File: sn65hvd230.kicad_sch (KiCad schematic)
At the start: 1 part, among them U6 SN65HVD230

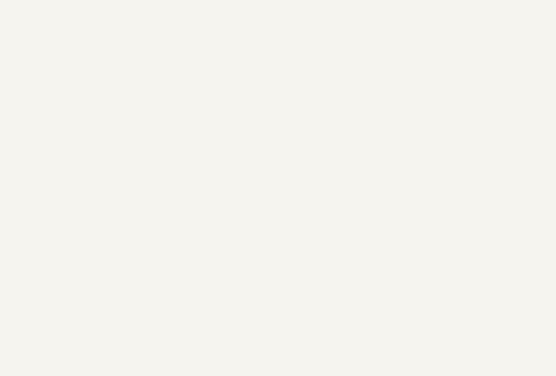
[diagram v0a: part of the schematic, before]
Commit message: feat: done rough board placements for general shape
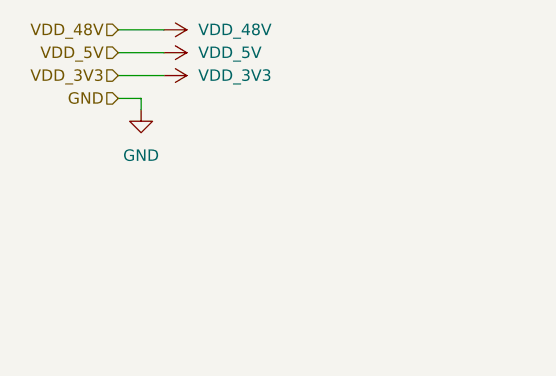
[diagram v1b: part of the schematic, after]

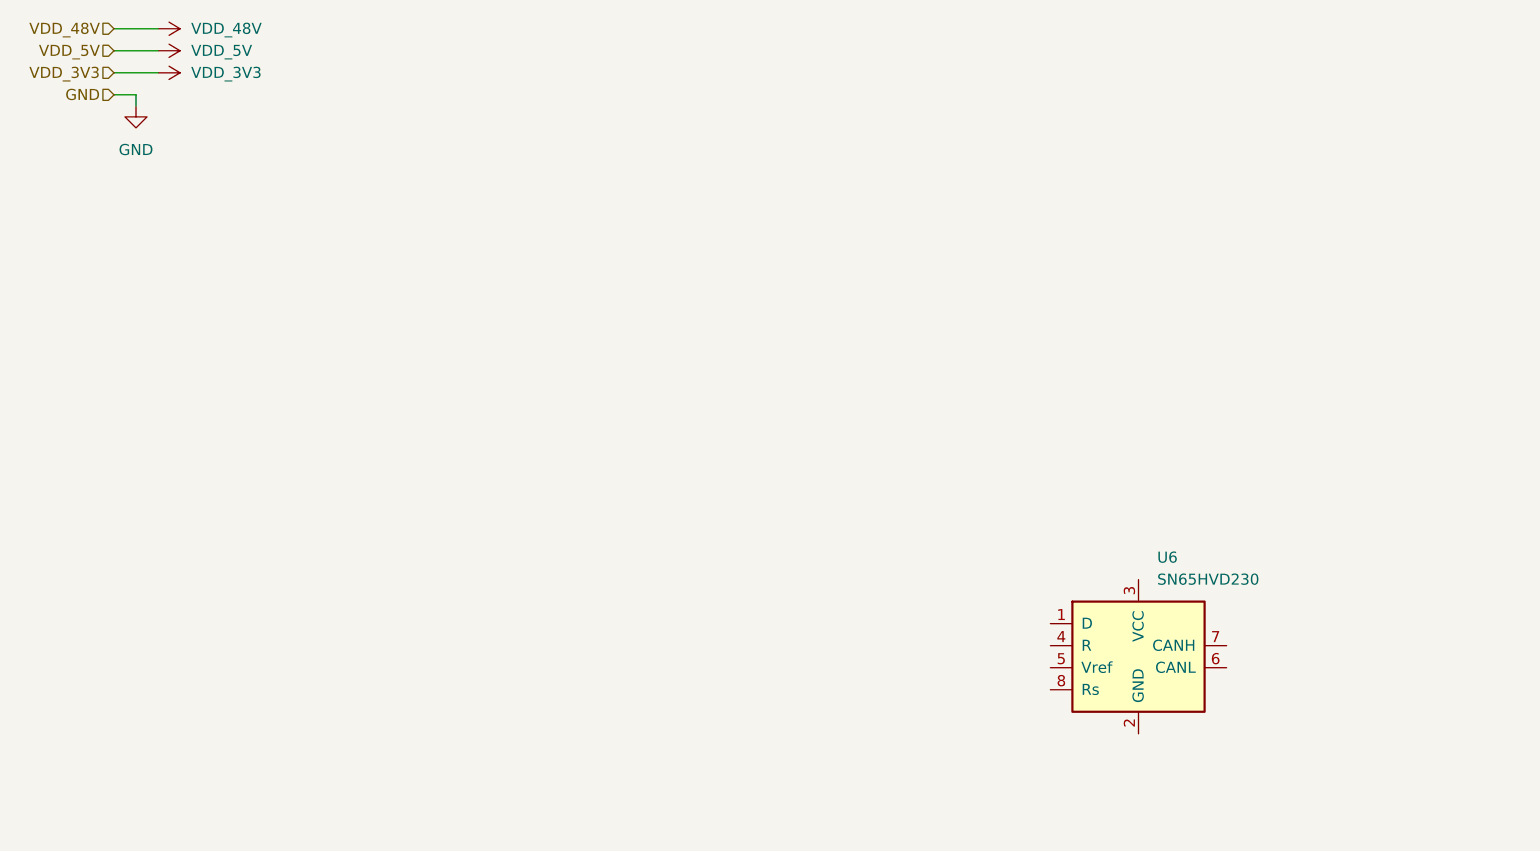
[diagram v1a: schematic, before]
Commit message: fix: fleshignout schematic for mcu, fpga and mag + peripherals
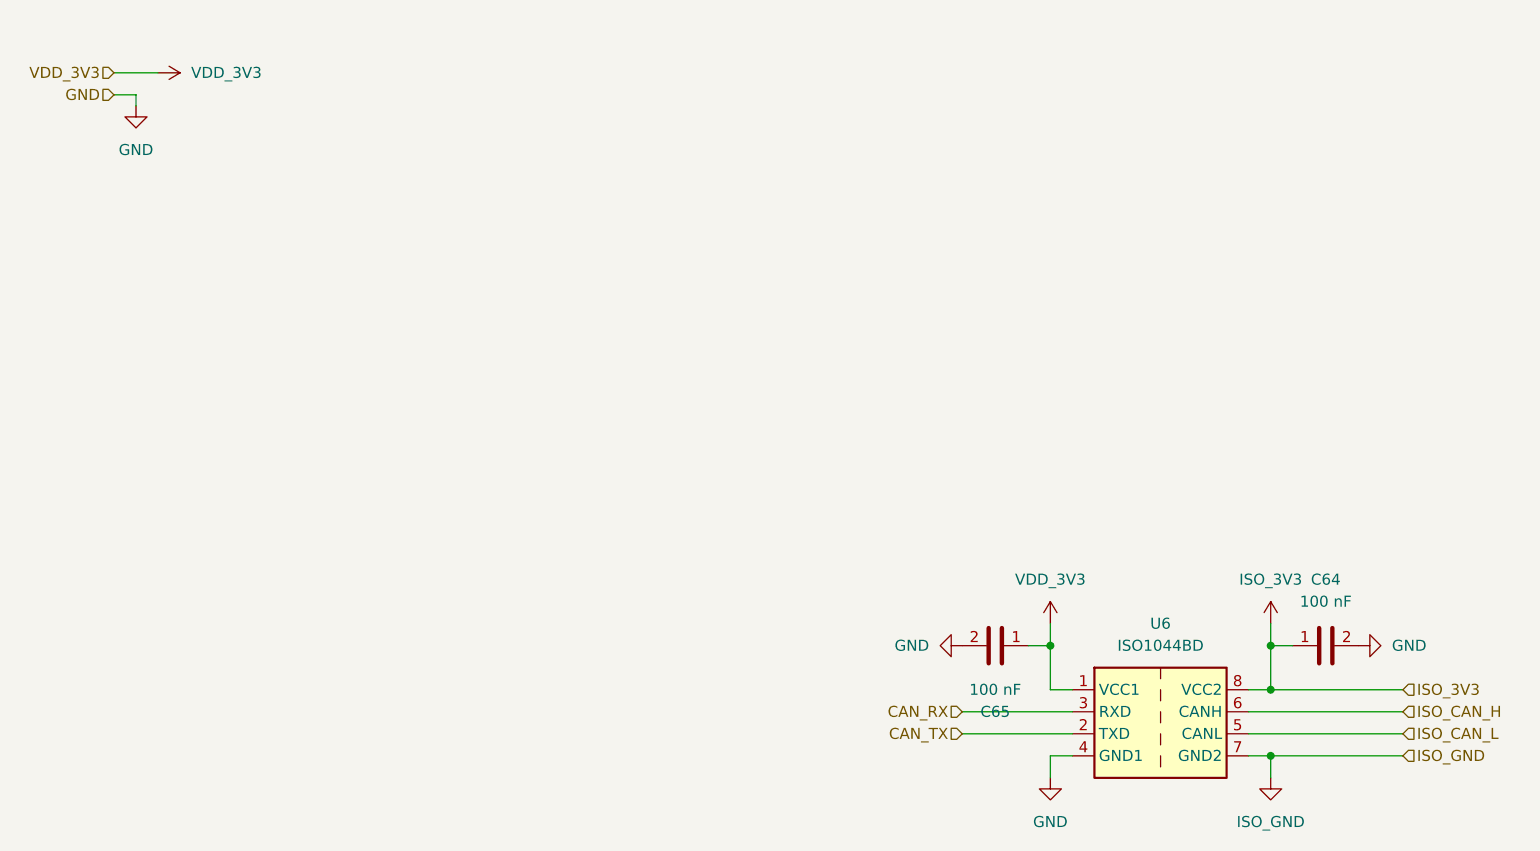
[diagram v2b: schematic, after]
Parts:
- removed U6: SN65HVD230, Package_SO:SOIC-8_3.9x4.9mm_P1.27mm, symbol Interface_CAN_LIN:SN65HVD230
- added C64, C65: 100 nF, chenry-footprint-lib:C_0402, symbol 0-chenry-component-lib:C_0402_100N
- added U6: ISO1044BD, Package_SO:SOIC-8_3.9x4.9mm_P1.27mm, symbol Interface_CAN_LIN:ISO1044BD
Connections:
- net GND: now also C64.2, C65.2, U6.4 (GND1)
- net VDD_3V3: now also C65.1, U6.1 (VCC1)
- new net CAN_RX: U6.3 (RXD)
- new net CAN_TX: U6.2 (TXD)
- new net ISO_3V3: C64.1, U6.8 (VCC2)
- new net ISO_CAN_H: U6.6 (CANH)
- new net ISO_CAN_L: U6.5 (CANL)
- new net ISO_GND: U6.7 (GND2)

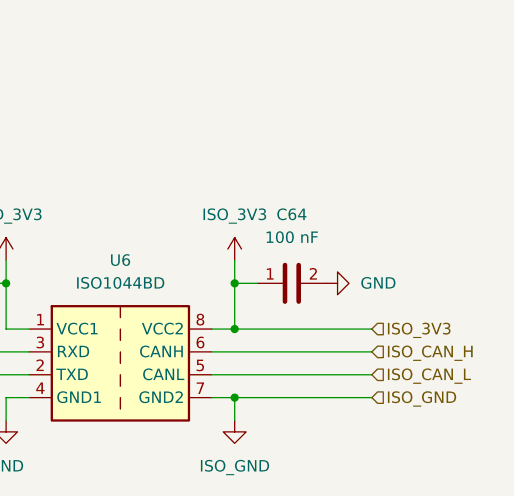
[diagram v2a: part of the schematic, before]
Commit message: fix: adjusting positioning of programmign header
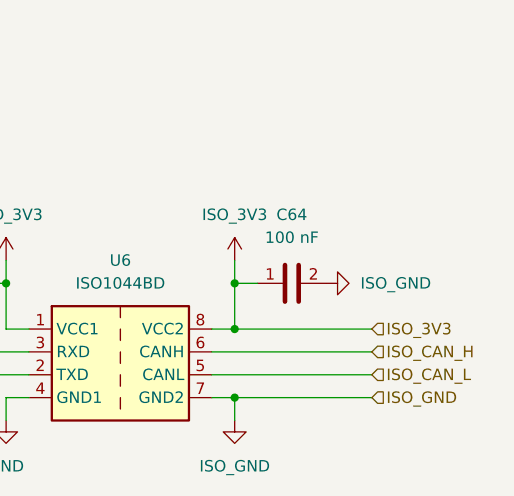
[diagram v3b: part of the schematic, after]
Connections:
- net GND: no longer C64.2
- net ISO_GND: now also C64.2
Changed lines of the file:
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@@
 	)
 	(symbol
-		(lib_id "power:GND")
+		(lib_id "power:GND2")
 		(at 170.18 87.63 90)
 		(unit 1)
@@
 			)
 		)
-		(property "Value" "GND"
+		(property "Value" "ISO_GND"
 			(at 173.99 87.6299 90)
 			(effects
@@
 			)
 		)
-		(property "Description" "Power symbol creates a global label with name \"GND\" , ground"
+		(property "Description" "Power symbol creates a global label with name \"GND2\" , ground"
 			(at 170.18 87.63 0)
 			(effects
+				(font
+					(size 1.27 1.27)
+				)
+				(hide yes)
+			)
+		)
+		(property "MFR_PN1" ""
+			(at 170.18 87.63 0)
+			(effects
+				(font
+					(size 1.27 1.27)
+				)
+				(hide yes)
+			)
+		)
+		(property "MFR_PN2" ""
+			(at 170.18 87.63 0)
+			(effects
+				(font
+					(size 1.27 1.27)
+				)
+				(hide yes)
+			)
+		)
+		(property "MFR_PN3" ""
+			(at 170.18 87.63 0)
+			(effects
+				(font
+					(size 1.27 1.27)
+				)
+				(hide yes)
+			)
+		)
+		(property "JLC_PN" ""
+			(at 170.18 87.63 0)
+			(effects
